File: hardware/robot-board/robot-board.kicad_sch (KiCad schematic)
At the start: 0 parts

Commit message: added "outline" for robot pcb
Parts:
- added Q3: BSS138, Package_TO_SOT_SMD:SOT-23, symbol Transistor_FET:BSS138
- added U1: ESP32-S3-WROOM-1, RF_Module:ESP32-S3-WROOM-1, symbol RF_Module:ESP32-S3-WROOM-1
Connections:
- new net: U1.1 (GND), U1.40 (GND), U1.41 (GND)
- new net USB_DM: U1.13 (USB_D-)
- new net USB_DP: U1.14 (USB_D+)
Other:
- note added: "3V3 Regulator"
- note added: "5V Regulator"
- note added: "Battery"
- note added: "Battery Monitor"
- note added: "ESD Protection"
- note added: "ESP32-S3-WROOM"
- note added: "Line Follower Breakout"
- note added: "Motor Drivers"
- note added: "Reset Button"
- note added: "Servos"
- note added: "Status LEDs"
- note added: "Step up PWM signal from 3.3V to 5V."
- note added: "USB-C Port"

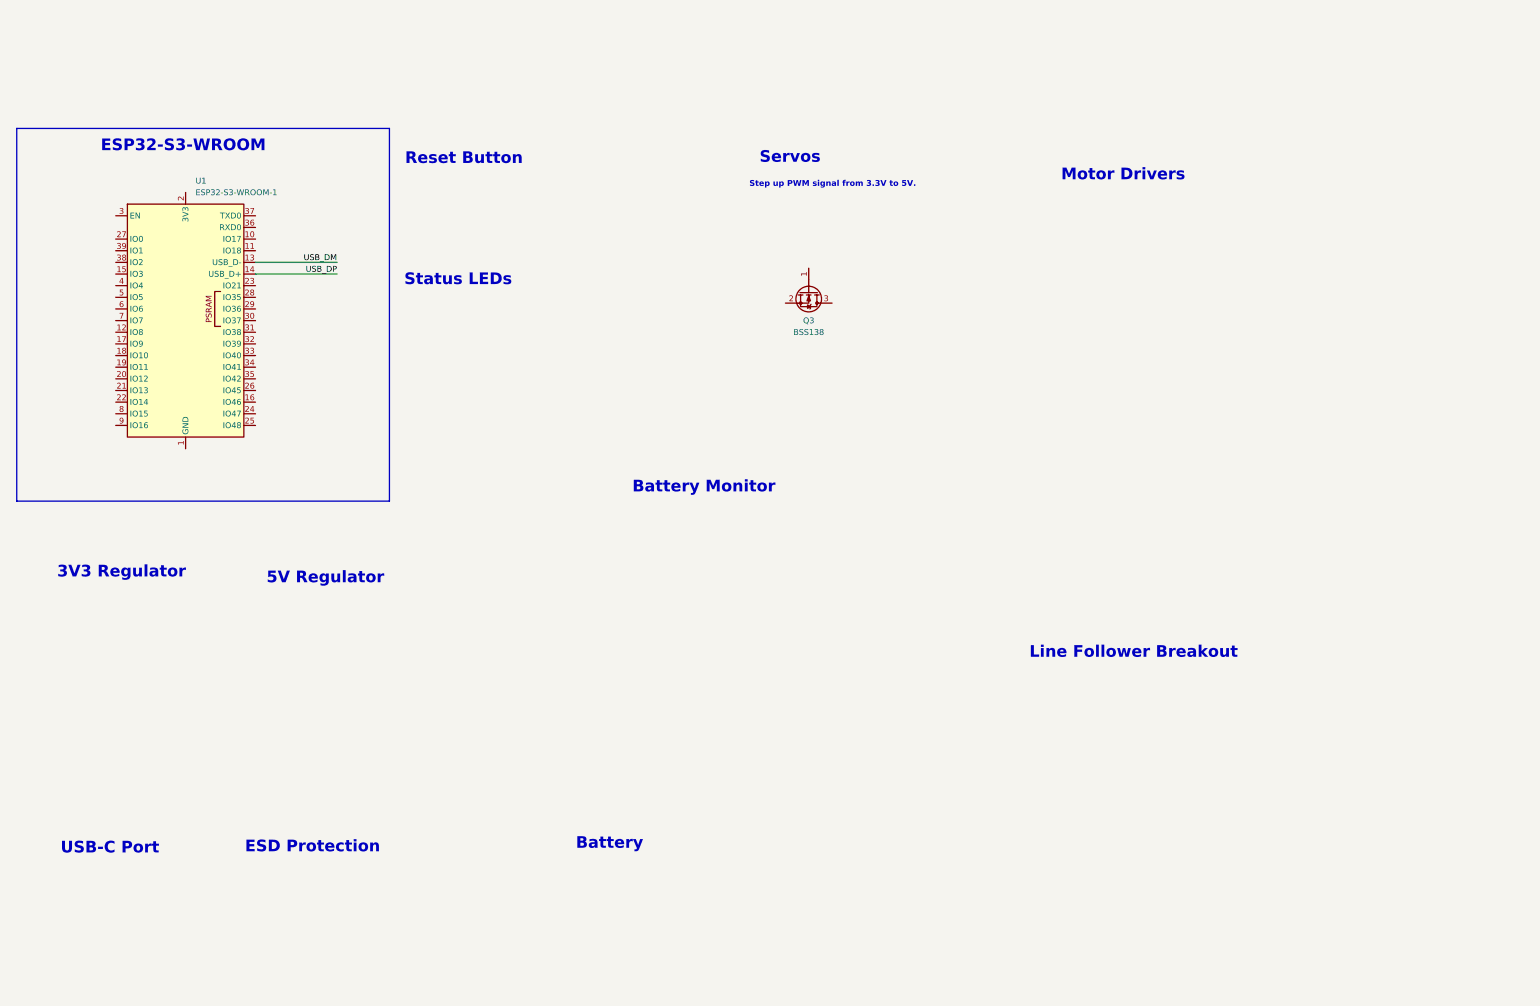
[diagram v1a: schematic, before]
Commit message: many changes
power management, status lights, servo control, BMS (waiting for mithun), ESD protection
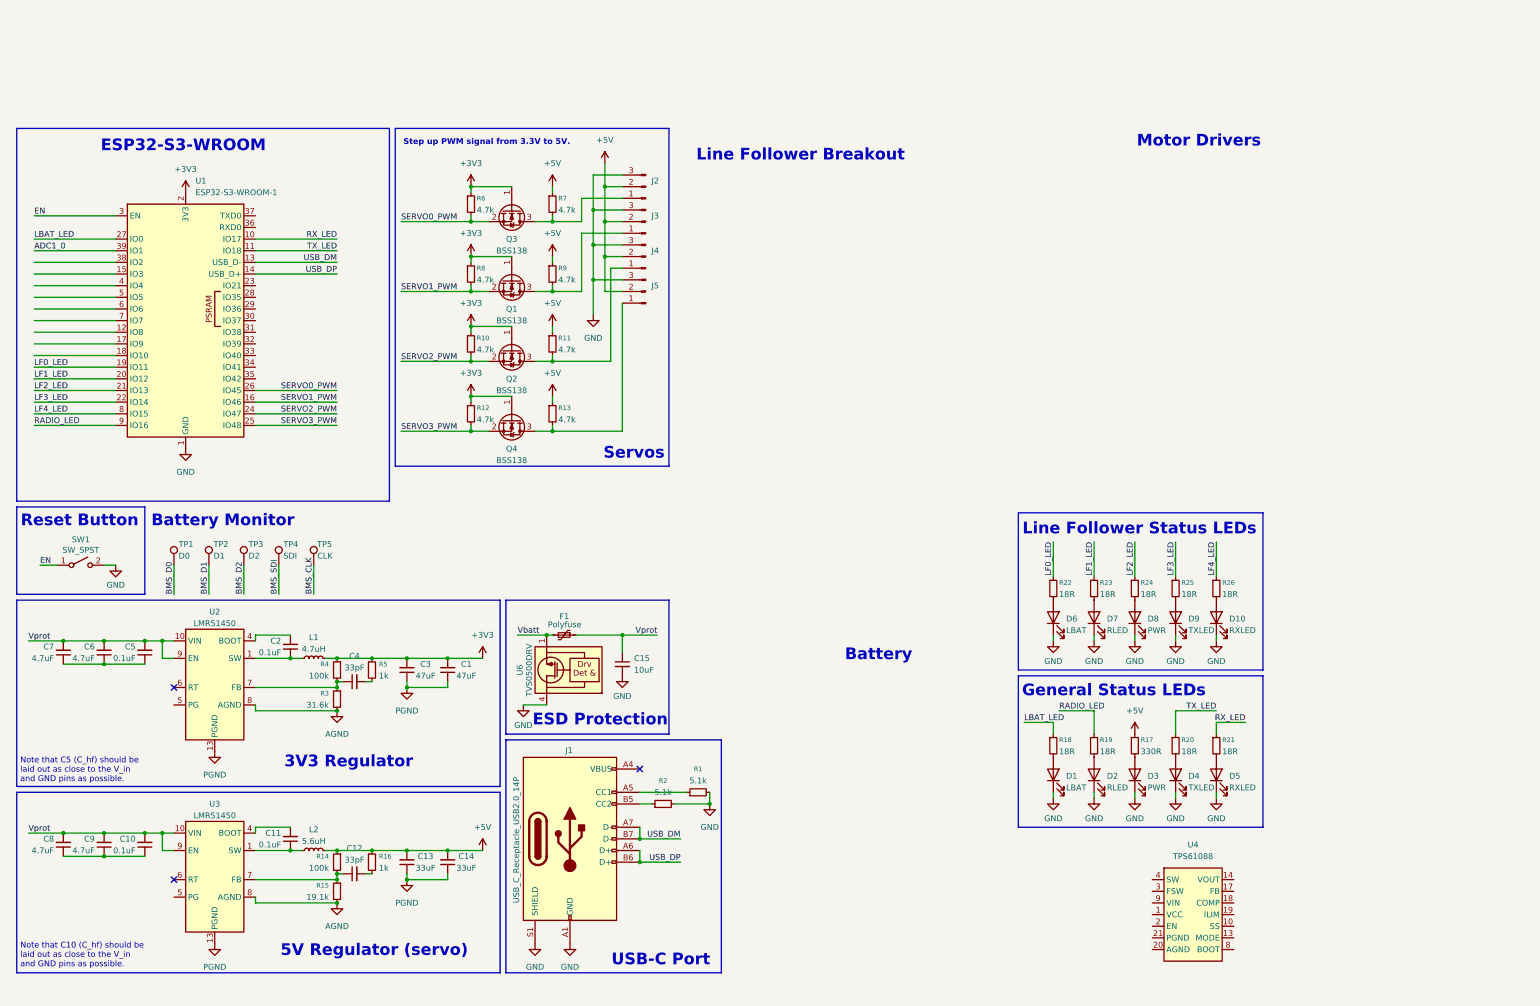
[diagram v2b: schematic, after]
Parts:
- added C1, C3: 47uF, symbol Device:C_Small
- added C10, C11, C2, C5: 0.1uF, symbol Device:C_Small
- added C12, C4: 33pF, symbol Device:C_Small
- added C13, C14: 33uF, symbol Device:C_Small
- added C15: 10uF, symbol Device:C_Small
- added C6, C7, C8, C9: 4.7uF, symbol Device:C_Small
- added D1, D6: LBAT, symbol Device:LED
- added D10, D5: RXLED, symbol Device:LED
- added D2, D7: RLED, symbol Device:LED
- added D3, D8: PWR, symbol Device:LED
- added D4, D9: TXLED, symbol Device:LED
- added F1: Polyfuse, Fuse:Fuse_Bourns_MF-SM_7.98x5.44mm, symbol Device:Polyfuse_Small
- added J1: USB_C_Receptacle_USB2.0_14P, symbol Connector:USB_C_Receptacle_USB2.0_14P
- added J2, J3, J4, J5: Conn_01x03_Pin, symbol Connector:Conn_01x03_Pin
- added L1: 4.7uH, symbol Device:L_Small
- added L2: 5.6uH, symbol Device:L_Small
- added Q1, Q2, Q4: BSS138, Package_TO_SOT_SMD:SOT-23, symbol Transistor_FET:BSS138
- added R1, R2: 5.1k, symbol Device:R_Small
- added R10, R11, R12, R13, R6, R7, R8, R9: 4.7k, symbol Device:R_Small
- added R14, R4: 100k, symbol Device:R_Small
- added R15: 19.1k, symbol Device:R_Small
- added R16, R5: 1k, symbol Device:R_Small
- added R17: 330R, symbol Device:R_Small
- added R18, R19, R20, R21, R22, R23, R24, R25, R26: 18R, symbol Device:R_Small
- added R3: 31.6k, symbol Device:R_Small
- added SW1: SW_SPST, symbol Switch:SW_SPST
- added TP1: D0, TestPoint:TestPoint_THTPad_2.0x2.0mm_Drill1.0mm, symbol Connector:TestPoint
- added TP2: D1, TestPoint:TestPoint_THTPad_2.0x2.0mm_Drill1.0mm, symbol Connector:TestPoint
- added TP3: D2, TestPoint:TestPoint_THTPad_2.0x2.0mm_Drill1.0mm, symbol Connector:TestPoint
- added TP4: SDI, TestPoint:TestPoint_THTPad_2.0x2.0mm_Drill1.0mm, symbol Connector:TestPoint
- added TP5: CLK, TestPoint:TestPoint_THTPad_2.0x2.0mm_Drill1.0mm, symbol Connector:TestPoint
- added U2, U3: LMR51450, Package_SON:WSON-12-1EP_3x3mm_P0.5mm_EP1.5x2.5mm, symbol Regulator_Switching:LMR51450
- added U4: TPS61088, Package_DFN_QFN:Texas_VQFN-RHL-20_ThermalVias, symbol Regulator_Switching:TPS61088
- added U6: TVS0500DRV, Package_SON:WSON-6-1EP_2x2mm_P0.65mm_EP1x1.6mm, symbol Power_Protection:TVS0500DRV
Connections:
- net USB_DM: now also J1.A7 (D-), J1.B7 (D-)
- net USB_DP: now also J1.A6 (D+), J1.B6 (D+)
- net +3V3: now reaches Q3.1 (G)
- net +3V3: now also U1.2 (3V3), C1.2, C3.2, L1.2, Q1.1 (G), Q2.1 (G), Q4.1 (G), R10.1, R12.1, R4.1, R5.1, R6.1, R8.1
- net SERVO0_PWM: now reaches Q3.2 (S)
- net SERVO0_PWM: now also U1.26 (IO45), R6.2
- net at Q3.3 (D): now also J2.1 (Pin_1), R7.2
- net GND: now reaches U1.1 (GND), U1.40 (GND), U1.41 (GND)
- net GND: now also C15.2, D1.1 (K), D10.1 (K), D2.1 (K), D3.1 (K), D4.1 (K), D5.1 (K), D6.1 (K), D7.1 (K), D8.1 (K), D9.1 (K), J1.A1 (GND), J1.A12 (GND), J1.B1 (GND), J1.B12 (GND), J1.S1 (SHIELD), J2.3 (Pin_3), J3.3 (Pin_3), J4.3 (Pin_3), J5.3 (Pin_3), R1.2, R2.2, SW1.2 (B), U6.4 (IN), U6.5 (IN), U6.6 (IN)
- net RX_LED: now reaches U1.10 (IO17)
- net RX_LED: now also R21.1
- net TX_LED: now reaches U1.11 (IO18)
- net TX_LED: now also R20.1
- net SERVO1_PWM: now reaches U1.16 (IO46)
- net SERVO1_PWM: now also Q1.2 (S), R8.2
- net LF0_LED: now reaches U1.19 (IO11)
- net LF0_LED: now also R22.1
- net LF1_LED: now reaches U1.20 (IO12)
- net LF1_LED: now also R23.1
- net LF2_LED: now reaches U1.21 (IO13)
- net LF2_LED: now also R24.1
- net LF3_LED: now reaches U1.22 (IO14)
- net LF3_LED: now also R25.1
- net SERVO2_PWM: now reaches U1.24 (IO47)
- net SERVO2_PWM: now also Q2.2 (S), R10.2
- net SERVO3_PWM: now reaches U1.25 (IO48)
- net SERVO3_PWM: now also Q4.2 (S), R12.2
- net LBAT_LED: now reaches U1.27 (IO0)
- net LBAT_LED: now also R18.1
- net EN: now reaches U1.3 (EN)
- net EN: now also SW1.1 (A)
- net ADC1_0: now reaches U1.39 (IO1)
- net LF4_LED: now reaches U1.8 (IO15)
- net LF4_LED: now also R26.1
- net RADIO_LED: now reaches U1.9 (IO16)
- net RADIO_LED: now also R19.1
- new net: J3.1 (Pin_1), Q1.3 (D), R9.2
- new net: D7.2 (A), R23.2
- new net: C12.1, R14.2, R15.1, U3.7 (FB)
- new net: C5.1, C6.1, C7.1
- new net: C2.1, L1.1, U2.1 (SW), U2.2 (SW), U2.3 (SW)
- new net: C2.2, U2.4 (BOOT)
- new net: C4.1, R3.1, R4.2, U2.7 (FB)
- new net: D9.2 (A), R25.2
- new net: D8.2 (A), R24.2
- new net: C11.1, L2.1, U3.1 (SW), U3.2 (SW), U3.3 (SW)
- new net: C11.2, U3.4 (BOOT)
- new net: C12.2, R16.2
- new net: J5.1 (Pin_1), Q4.3 (D), R13.2
- new net: J4.1 (Pin_1), Q2.3 (D), R11.2
- new net: D6.2 (A), R22.2
- new net: U4.11 (NC), U4.12 (NC)
- new net: U4.14 (VOUT), U4.15 (VOUT), U4.16 (VOUT)
- new net: U4.4 (SW), U4.5 (SW), U4.6 (SW), U4.7 (SW)
- new net: D1.2 (A), R18.2
- new net: D5.2 (A), R21.2
- new net: J1.B5 (CC2), R2.1
- new net: D3.2 (A), R17.2
- new net: D4.2 (A), R20.2
- new net: D10.2 (A), R26.2
- new net: C10.1, C8.1, C9.1
- new net: J1.A5 (CC1), R1.1
- new net: D2.2 (A), R19.2
- new net: C4.2, R5.2
- new net: J1.A4 (VBUS), J1.A9 (VBUS), J1.B4 (VBUS), J1.B9 (VBUS)
- new net +5V: C13.2, C14.2, J2.2 (Pin_2), J3.2 (Pin_2), J4.2 (Pin_2), J5.2 (Pin_2), L2.2, R11.1, R13.1, R14.1, R16.1, R17.1, R7.1, R9.1
- new net AGND: R15.2, R3.2, U2.8 (AGND), U3.8 (AGND)
- new net BMS_CLK: TP5.1
- new net BMS_D0: TP1.1
- new net BMS_D1: TP2.1
- new net BMS_D2: TP3.1
- new net BMS_SDI: TP4.1
- new net PGND: C1.1, C13.1, C14.1, C3.1, U2.13 (PGND), U3.13 (PGND)
- new net VIN: C10.2, C15.1, C5.2, C6.2, C7.2, C8.2, C9.2, F1.1, U2.10 (VIN), U2.11 (VIN), U2.12 (VIN), U2.9 (EN), U3.10 (VIN), U3.11 (VIN), U3.12 (VIN), U3.9 (EN)
- new net Vbatt: F1.2, U6.1 (GND), U6.2 (GND), U6.3 (GND), U6.7 (GND)
- no-connect marks 0 -> 3
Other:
- note added: "5V Regulator (servo)"
- note added: "General Status LEDs"
- note added: "Line Follower Status LEDs"
- note added: "Note that C10 (C_hf) should be laid out as close to the V_in and GND pins as possible."
- note added: "Note that C5 (C_hf) should be laid out as close to the V_in and GND pins as possible."
- note removed: "5V Regulator"
- note removed: "Status LEDs"
- company: (none) -> Carnegie Mellon Robotics Club
- title: (none) -> Red Robot 26+ Mainboard
- moved on the sheet: Q3
